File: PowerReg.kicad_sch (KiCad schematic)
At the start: 8 parts

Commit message: Assigned almost all footprints
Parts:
- C44, C46: footprint (none) -> Capacitor_SMD:C_0603_1608Metric; Part # (none) -> Generic 0603 1uF 6.3V X7R MLCC
- C45, C47: footprint (none) -> Capacitor_SMD:C_0603_1608Metric; Part # (none) -> Generic 0603 0.1uF 6.3V X7R MLCC
- U32, U33: footprint (none) -> Converter_DCDC:Converter_DCDC_TRACO_TSR-1_THT
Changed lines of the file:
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@@
 			)
 		)
-		(property "Footprint" ""
+		(property "Footprint" "Capacitor_SMD:C_0603_1608Metric"
 			(at 172.72 97.79 0)
 			(effects
@@
 		)
 		(property "Description" "Unpolarized capacitor, small symbol"
+			(at 172.72 97.79 0)
+			(effects
+				(font
+					(size 1.27 1.27)
+				)
+				(hide yes)
+			)
+		)
+		(property "Part #" "Generic 0603 1uF 6.3V X7R MLCC"
 			(at 172.72 97.79 0)
 			(effects
@@
 			)
 		)
-		(property "Footprint" ""
+		(property "Footprint" "Capacitor_SMD:C_0603_1608Metric"
 			(at 149.86 97.79 0)
 			(effects
@@
 		)
 		(property "Description" "Unpolarized capacitor, small symbol"
+			(at 149.86 97.79 0)
+			(effects
+				(font
+					(size 1.27 1.27)
+				)
+				(hide yes)
+			)
+		)
+		(property "Part #" "Generic 0603 0.1uF 6.3V X7R MLCC"
 			(at 149.86 97.79 0)
 			(effects
@@
 			)
 		)
-		(property "Footprint" ""
+		(property "Footprint" "Capacitor_SMD:C_0603_1608Metric"
 			(at 193.04 97.79 0)
 			(effects
@@
 		)
 		(property "Description" "Unpolarized capacitor, small symbol"
+			(at 193.04 97.79 0)
+			(effects
+				(font
+					(size 1.27 1.27)
+				)
+				(hide yes)
+			)
+		)
+		(property "Part #" "Generic 0603 0.1uF 6.3V X7R MLCC"
 			(at 193.04 97.79 0)
 			(effects
@@
 			)
 		)
-		(property "Footprint" ""
+		(property "Footprint" "Capacitor_SMD:C_0603_1608Metric"
 			(at 129.54 97.79 0)
 			(effects
@@
 		)
 		(property "Description" "Unpolarized capacitor, small symbol"
+			(at 129.54 97.79 0)
+			(effects
+				(font
+					(size 1.27 1.27)
+				)
+				(hide yes)
+			)
+		)
+		(property "Part #" "Generic 0603 1uF 6.3V X7R MLCC"
 			(at 129.54 97.79 0)
 			(effects
@@
 			)
 		)
-		(property "Footprint" ""
+		(property "Footprint" "Converter_DCDC:Converter_DCDC_TRACO_TSR-1_THT"
 			(at 139.7 85.09 0)
 			(effects
@@
 			)
 		)
-		(property "Footprint" ""
+		(property "Footprint" "Converter_DCDC:Converter_DCDC_TRACO_TSR-1_THT"
 			(at 182.88 85.09 0)
 			(effects

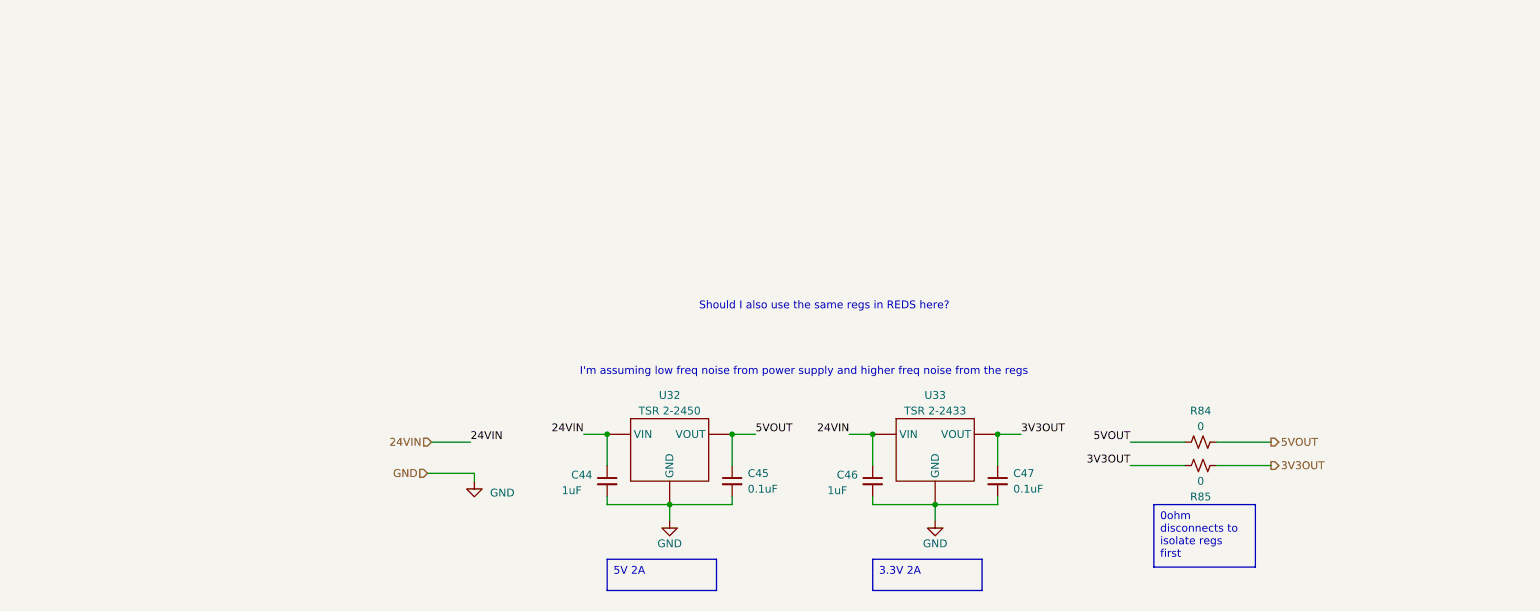
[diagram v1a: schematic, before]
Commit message: Replaced Regs
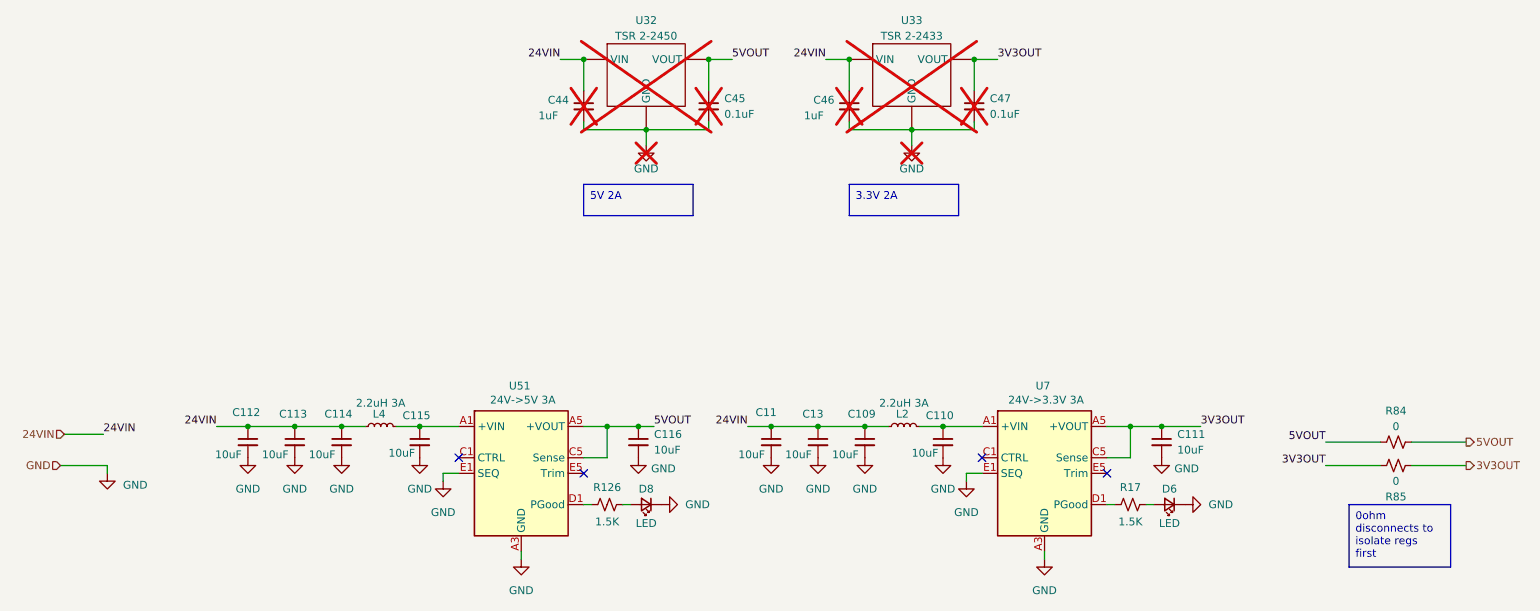
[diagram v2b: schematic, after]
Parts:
- added C109, C11, C110, C112, C113, C114, C115, C13: 10uF, Capacitor_SMD:C_1210_3225Metric, symbol Device:C_Small
- added C111, C116: 10uF, Capacitor_SMD:C_1206_3216Metric, symbol Device:C_Small
- added D6, D8: LED, LED_SMD:LED_0603_1608Metric_Pad1.05x0.95mm_HandSolder, symbol Device:LED_Small
- added L2, L4: 2.2uH 3A, Inductor_SMD:L_Vishay_IHLP-1212, symbol Device:L_Small
- added R126, R17: 1.5K, Resistor_SMD:R_0402_1005Metric, symbol Device:R_Small_US
- added U51: 24V->5V 3A, Converter_DCDC:Converter_DCDC_RECOM_RPMx.x-x.0, symbol Converter_DCDC:RPM3.3-6.0
- added U7: 24V->3.3V 3A, Converter_DCDC:Converter_DCDC_RECOM_RPMx.x-x.0, symbol Converter_DCDC:RPM3.3-6.0
- C44, C45, C46, C47, U32, U33: now not fitted; now left out of the parts list
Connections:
- net 24VIN: now also C109.1, C11.1, C112.1, C113.1, C114.1, C13.1, L2.1, L4.1
- net 3V3OUT: now also C111.1, U7.A5 (+VOUT), U7.B5 (+VOUT), U7.C5 (Sense)
- net 5VOUT: now also C116.1, U51.A5 (+VOUT), U51.B5 (+VOUT), U51.C5 (Sense)
- net GND: now also C109.2, C11.2, C110.2, C111.2, C112.2, C113.2, C114.2, C115.2, C116.2, C13.2, D6.1 (K), D8.1 (K), U51.A3 (GND), U51.A4 (GND), U51.B1 (GND), U51.B2 (GND), U51.B3 (GND), U51.B4 (GND), U51.C2 (GND), U51.C3 (GND), U51.C4 (GND), U51.D2 (GND), U51.D3 (GND), U51.D4 (GND), U51.D5 (GND), U51.E1 (SEQ), U51.E3 (GND), U51.E4 (GND), U7.A3 (GND), U7.A4 (GND), U7.B1 (GND), U7.B2 (GND), U7.B3 (GND), U7.B4 (GND), U7.C2 (GND), U7.C3 (GND), U7.C4 (GND), U7.D2 (GND), U7.D3 (GND), U7.D4 (GND), U7.D5 (GND), U7.E1 (SEQ), U7.E3 (GND), U7.E4 (GND)
- new net: C110.1, L2.2, U7.A1 (+VIN), U7.A2 (+VIN)
- new net: C115.1, L4.2, U51.A1 (+VIN), U51.A2 (+VIN)
- new net: R126.1, U51.D1 (PGood)
- new net: D8.2 (A), R126.2
- new net: D6.2 (A), R17.2
- new net: R17.1, U7.D1 (PGood)
- no-connect marks 0 -> 4
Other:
- note removed: "I'm assuming low freq noise from power supply and higher freq noise from the regs"
- note removed: "Should I also use the same regs in REDS here?"
- moved on the sheet: R84, R85

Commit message: Finished layout
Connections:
- net 3V3OUT: no longer C111.1, R85.1, U7.A5 (+VOUT), U7.B5 (+VOUT), U7.C5 (Sense)
- net 5VOUT: no longer C116.1, R84.1, U51.A5 (+VOUT), U51.B5 (+VOUT), U51.C5 (Sense)
- new net: C111.1, R85.1, U7.A5 (+VOUT), U7.B5 (+VOUT), U7.C5 (Sense)
- new net: C116.1, R84.1, U51.A5 (+VOUT), U51.B5 (+VOUT), U51.C5 (Sense)
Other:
- moved on the sheet: R84, R85
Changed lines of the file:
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@@
 	(wire
 		(pts
-			(xy 134.62 88.9) (xy 137.16 88.9)
+			(xy 134.62 88.9) (xy 135.89 88.9)
 		)
 		(stroke
@@
 	(wire
 		(pts
-			(xy 260.35 91.44) (xy 269.24 91.44)
+			(xy 149.86 81.28) (xy 158.75 81.28)
 		)
 		(stroke
@@
 	(wire
 		(pts
-			(xy 219.71 88.9) (xy 226.06 88.9)
+			(xy 135.89 81.28) (xy 135.89 88.9)
+		)
+		(stroke
+			(width 0)
+			(type default)
+		)
+	)
+	(wire
+		(pts
+			(xy 219.71 88.9) (xy 238.76 88.9)
 		)
 		(stroke
@@
 	(wire
 		(pts
-			(xy 246.38 91.44) (xy 255.27 91.44)
+			(xy 135.89 81.28) (xy 144.78 81.28)
 		)
 		(stroke
@@
 	(wire
 		(pts
-			(xy 246.38 95.25) (xy 255.27 95.25)
-		)
-		(stroke
-			(width 0)
-			(type default)
-		)
-	)
-	(wire
-		(pts
-			(xy 260.35 95.25) (xy 269.24 95.25)
+			(xy 243.84 88.9) (xy 252.73 88.9)
 		)
 		(stroke
@@
 	(text_box "0ohm disconnects to isolate regs first"
 		(exclude_from_sim no)
-		(at 250.19 101.6 0)
+		(at 233.68 95.25 0)
 		(size 16.51 10.16)
 		(stroke
@@
 	)
 	(label "3V3OUT"
-		(at 246.38 95.25 180)
+		(at 193.04 29.21 0)
 		(fields_autoplaced yes)
 		(effects
@@
 				(size 1.27 1.27)
 			)
-			(justify right bottom)
-		)
-	)
-	(label "5VOUT"
-		(at 246.38 91.44 180)
+			(justify left bottom)
+		)
+	)
+	(label "24VIN"
+		(at 121.92 29.21 180)
 		(fields_autoplaced yes)
 		(effects
@@
 		)
 	)
-	(label "3V3OUT"
-		(at 193.04 29.21 0)
+	(label "24VIN"
+		(at 47.625 90.17 0)
 		(fields_autoplaced yes)
 		(effects
@@
 		)
 	)
-	(label "5VOUT"
-		(at 137.16 88.9 0)
+	(label "24VIN"
+		(at 165.1 29.21 180)
 		(fields_autoplaced yes)
 		(effects
@@
 				(size 1.27 1.27)
 			)
-			(justify left bottom)
+			(justify right bottom)
 		)
 	)
 	(label "24VIN"
-		(at 121.92 29.21 180)
+		(at 66.04 88.9 180)
 		(fields_autoplaced yes)
 		(effects
@@
 		)
 	)
-	(label "24VIN"
-		(at 47.625 90.17 0)
+	(label "5VOUT"
+		(at 149.86 29.21 0)
 		(fields_autoplaced yes)
 		(effects
@@
 		)
 	)
-	(label "3V3OUT"
-		(at 226.06 88.9 0)
+	(hierarchical_label "5VOUT"
+		(shape output)
+		(at 158.75 81.28 0)
 		(fields_autoplaced yes)
 		(effects
@@
 				(size 1.27 1.27)
 			)
-			(justify left bottom)
-		)
-	)
-	(label "24VIN"
-		(at 165.1 29.21 180)
+			(justify left)
+		)
+	)
+	(hierarchical_label "24VIN"
+		(shape input)
+		(at 41.275 90.17 180)
 		(fields_autoplaced yes)
 		(effects
@@
 				(size 1.27 1.27)
 			)
-			(justify right bottom)
-		)
-	)
-	(label "24VIN"
-		(at 66.04 88.9 180)
-		(fields_autoplaced yes)
-		(effects
-			(font
-				(size 1.27 1.27)
-			)
-			(justify right bottom)
-		)
-	)
-	(label "5VOUT"
-		(at 149.86 29.21 0)
-		(fields_autoplaced yes)
-		(effects
-			(font
-				(size 1.27 1.27)
-			)
-			(justify left bottom)
-		)
-	)
-	(hierarchical_label "5VOUT"
-		(shape output)
-		(at 269.24 91.44 0)
-		(fields_autoplaced yes)
-		(effects
-			(font
-				(size 1.27 1.27)
-			)
-			(justify left)
-		)
-	)
-	(hierarchical_label "24VIN"
-		(shape input)
-		(at 41.275 90.17 180)
-		(fields_autoplaced yes)
-		(effects
-			(font
-				(size 1.27 1.27)
-			)
 			(justify right)
 		)
@@
 	(hierarchical_label "3V3OUT"
 		(shape output)
-		(at 269.24 95.25 0)
+		(at 252.73 88.9 0)
 		(fields_autoplaced yes)
 		(effects
@@
 	(symbol
 		(lib_id "Device:R_Small_US")
-		(at 257.81 95.25 90)
+		(at 241.3 88.9 90)
 		(unit 1)
 		(exclude_from_sim no)
@@
 		(dnp no)
 		(property "Reference" "R85"
-			(at 257.81 100.33 90)
+			(at 241.3 93.98 90)
 			(effects
 				(font
@@
 		)
 		(property "Value" "0"
-			(at 257.81 97.79 90)
+			(at 241.3 91.44 90)
 			(effects
 				(font
@@
 		)
 		(property "Footprint" "Resistor_SMD:R_1206_3216Metric_Pad1.30x1.75mm_HandSolder"
-			(at 257.81 95.25 0)
+			(at 241.3 88.9 0)
 			(effects
 				(font
@@
 		)
 		(property "Datasheet" "~"
-			(at 257.81 95.25 0)
+			(at 241.3 88.9 0)
 			(effects
 				(font
@@
 		)
 		(property "Description" ""
-			(at 257.81 95.25 0)
+			(at 241.3 88.9 0)
 			(effects
 				(font
@@
 	(symbol
 		(lib_id "Device:R_Small_US")
-		(at 257.81 91.44 90)
+		(at 147.32 81.28 90)
 		(unit 1)
 		(exclude_from_sim no)
@@
 		(on_board yes)
 		(dnp no)
-		(fields_autoplaced yes)
 		(property "Reference" "R84"
-			(at 257.81 86.36 90)
+			(at 147.32 76.2 90)
 			(effects
 				(font
@@
 		)
 		(property "Value" "0"
-			(at 257.81 88.9 90)
+			(at 147.32 78.74 90)
 			(effects
 				(font
@@
 		)
 		(property "Footprint" "Resistor_SMD:R_1206_3216Metric_Pad1.30x1.75mm_HandSolder"
-			(at 257.81 91.44 0)
+			(at 147.32 81.28 0)
 			(effects
 				(font
@@
 		)
 		(property "Datasheet" "~"
-			(at 257.81 91.44 0)
+			(at 147.32 81.28 0)
 			(effects
 				(font
@@
 		)
 		(property "Description" ""
-			(at 257.81 91.44 0)
-			(effects
-				(font
+			(at 147.32 81.28 0)
+			(effects
+				(font

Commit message: new BOM
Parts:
- C109, C11, C110, C112, C113, C114, C115, C13: Manufacturer (none) -> Generic; Part # (none) -> Generic CAP CER 10UF 50V X7R 1210
- C111, C116: Manufacturer (none) -> Generic; Part # (none) -> Generic CAP CER 10UF 25V X7R 1206
- C44, C46: Manufacturer (none) -> Generic; Part # Generic 0603 1uF 6.3V X7R MLCC -> Generic CAP CER 1UF 50V X7R 0603
- C45, C47: Manufacturer (none) -> Generic; Part # Generic 0603 0.1uF 6.3V X7R MLCC -> Generic CAP CER 0.1UF 6.3V X7R 0603
- R126, R17: Part # Generic 0402 1.5K 0.1% Resistor -> Generic RES SMD 1.5K OHM 0.1% 1/16W 0402
- R84, R85: Manufacturer (none) -> Generic; Part # (none) -> Generic RES SMD 0 OHM 1206
- U51, U7: Manufacturer RECOM -> Recom Power

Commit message: REDS updated with diodes and hierarchy to main micro
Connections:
- net 3V3OUT renamed 3V3_REDSOUT

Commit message: Component placement halfway done
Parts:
- added TP25: 5V, TestPoint:TestPoint_Plated_Hole_D2.0mm, symbol Connector:TestPoint
- added TP26: 3.3V, TestPoint:TestPoint_Plated_Hole_D2.0mm, symbol Connector:TestPoint
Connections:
- net at C111.1, R85.1, U7.A5 (+VOUT)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: now also TP26.1
- net at C116.1, R84.1, U51.A5 (+VOUT)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: now also TP25.1
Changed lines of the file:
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@@
 		(color 0 0 0 0)
 	)
+	(junction
+		(at 135.89 81.28)
+		(diameter 0)
+		(color 0 0 0 0)
+	)
 	(no_connect
 		(at 190.5 93.98)
@@
 	)
 	(symbol
+		(lib_id "Connector:TestPoint")
+		(at 135.89 81.28 0)
+		(unit 1)
+		(exclude_from_sim no)
+		(in_bom yes)
+		(on_board yes)
+		(dnp no)
+		(fields_autoplaced yes)
+		(property "Reference" "TP25"
+			(at 138.43 76.7079 0)
+			(effects
+				(font
+					(size 1.27 1.27)
+				)
+				(justify left)
+			)
+		)
+		(property "Value" "5V"
+			(at 138.43 79.2479 0)
+			(effects
+				(font
+					(size 1.27 1.27)
+				)
+				(justify left)
+			)
+		)
+		(property "Footprint" "TestPoint:TestPoint_Plated_Hole_D2.0mm"
+			(at 140.97 81.28 0)
+			(effects
+				(font
+					(size 1.27 1.27)
+				)
+				(hide yes)
+			)
+		)
+		(property "Datasheet" "~"
+			(at 140.97 81.28 0)
+			(effects
+				(font
+					(size 1.27 1.27)
+				)
+				(hide yes)
+			)
+		)
+		(property "Description" "test point"
+			(at 135.89 81.28 0)
+			(effects
+				(font
+					(size 1.27 1.27)
+				)
+				(hide yes)
+			)
+		)
+		(pin "1"
+		)
+		(instances
+			(project "rocket2-ecu"
+				(path "/02606b2c-b376-4ffb-9781-f9cea3f70994/944e98dc-4249-4ad7-a352-e05a5cc42499"
+					(reference "TP25")
+					(unit 1)
+				)
+			)
+		)
+	)
+	(symbol
 		(lib_id "Device:R_Small_US")
 		(at 241.3 88.9 90)
@@
 					(unit 1)
 				)
+			)
+		)
+	)
+	(symbol
+		(lib_id "Connector:TestPoint")
+		(at 219.71 88.9 0)
+		(unit 1)
+		(exclude_from_sim no)
+		(in_bom yes)
+		(on_board yes)
+		(dnp no)
+		(fields_autoplaced yes)
+		(property "Reference" "TP26"
+			(at 222.25 84.3279 0)
+			(effects
+				(font
+					(size 1.27 1.27)
+				)
+				(justify left)
+			)
+		)
+		(property "Value" "3.3V"
+			(at 222.25 86.8679 0)
+			(effects
+				(font
+					(size 1.27 1.27)
+				)
+				(justify left)
+			)
+		)
+		(property "Footprint" "TestPoint:TestPoint_Plated_Hole_D2.0mm"
+			(at 224.79 88.9 0)
+			(effects
+				(font
+					(size 1.27 1.27)
+				)
+				(hide yes)
+			)
+		)
+		(property "Datasheet" "~"
+			(at 224.79 88.9 0)
+			(effects
+				(font
+					(size 1.27 1.27)
+				)
+				(hide yes)
+			)
+		)
+		(property "Description" "test point"
+			(at 219.71 88.9 0)
+			(effects
+				(font
+					(size 1.27 1.27)
+				)
+				(hide yes)
+			)
+		)
+		(pin "1"
+		)
+		(instances
+			(project "rocket2-ecu"
+				(path "/02606b2c-b376-4ffb-9781-f9cea3f70994/944e98dc-4249-4ad7-a352-e05a5cc42499"
+					(reference "TP26")
+					(unit 1)
+				)

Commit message: ALMOST
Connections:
- net 3.3V_out: now reaches C111.1, R85.1, TP26.1, U7.A5 (+VOUT), U7.B5 (+VOUT), U7.C5 (Sense)
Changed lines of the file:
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@@
+		(color 0 0 0 0)
+	)
+	(junction
+		(at 231.14 88.9)
+		(diameter 0)
 		(color 0 0 0 0)
 	)
@@
 	(wire
 		(pts
+			(xy 231.14 88.9) (xy 238.76 88.9)
+		)
+		(stroke
+			(width 0)
+			(type default)
+		)
+	)
+	(wire
+		(pts
 			(xy 165.1 29.21) (xy 168.91 29.21)
 		)
@@
 	(wire
 		(pts
-			(xy 219.71 88.9) (xy 238.76 88.9)
+			(xy 219.71 88.9) (xy 231.14 88.9)
 		)
 		(stroke
@@
 					(unit 1)
 				)
+			)
+		)
+	)
+	(symbol
+		(lib_id "power:+1V5")
+		(at 231.14 88.9 0)
+		(unit 1)
+		(exclude_from_sim no)
+		(in_bom yes)
+		(on_board yes)
+		(dnp no)
+		(fields_autoplaced yes)
+		(property "Reference" "#PWR0296"
+			(at 231.14 92.71 0)
+			(effects
+				(font
+					(size 1.27 1.27)
+				)
+				(hide yes)
+			)
+		)
+		(property "Value" "3.3V_out"
+			(at 231.14 83.82 0)
+			(effects
+				(font
+					(size 1.27 1.27)
+				)
+			)
+		)
+		(property "Footprint" ""
+			(at 231.14 88.9 0)
+			(effects
+				(font
+					(size 1.27 1.27)
+				)
+				(hide yes)
+			)
+		)
+		(property "Datasheet" ""
+			(at 231.14 88.9 0)
+			(effects
+				(font
+					(size 1.27 1.27)
+				)
+				(hide yes)
+			)
+		)
+		(property "Description" "Power symbol creates a global label with name \"+1V5\""
+			(at 231.14 88.9 0)
+			(effects
+				(font
+					(size 1.27 1.27)
+				)
+				(hide yes)
+			)
+		)
+		(pin "1"
+		)
+		(instances
+			(project ""
+				(path "/02606b2c-b376-4ffb-9781-f9cea3f70994/944e98dc-4249-4ad7-a352-e05a5cc42499"
+					(reference "#PWR0296")
+					(unit 1)
+				)

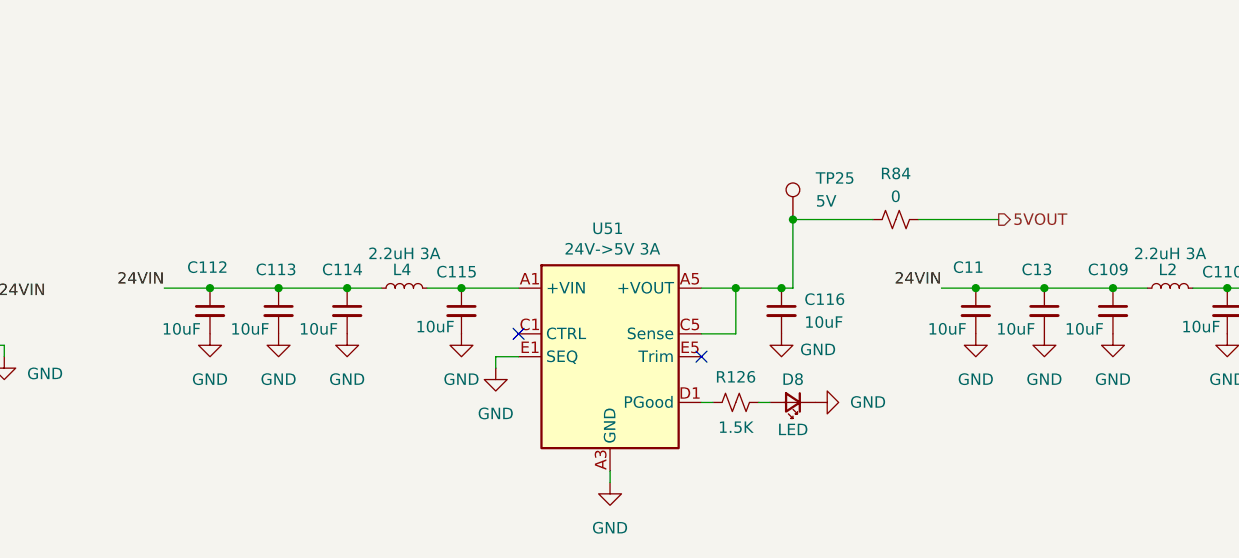
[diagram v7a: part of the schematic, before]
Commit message: Deleted 5V, edited LPFs on TCs and PTs
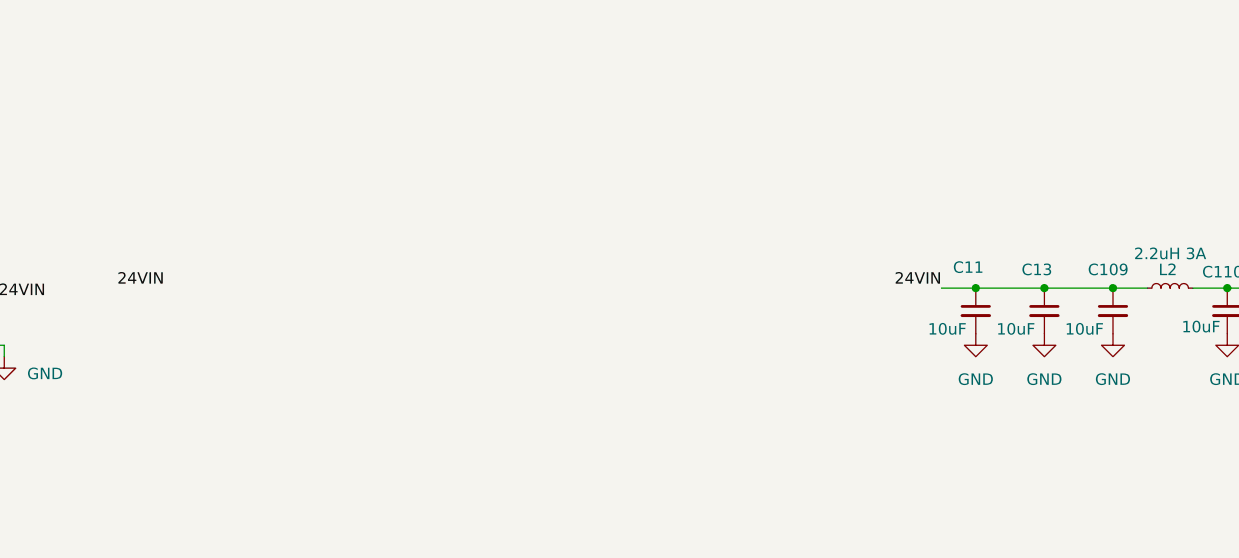
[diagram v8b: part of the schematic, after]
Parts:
- removed C112, C113, C114, C115: 10uF, Capacitor_SMD:C_1210_3225Metric, symbol Device:C_Small
- removed C116: 10uF, Capacitor_SMD:C_1206_3216Metric, symbol Device:C_Small
- removed D8: LED, LED_SMD:LED_0603_1608Metric_Pad1.05x0.95mm_HandSolder, symbol Device:LED_Small
- removed L4: 2.2uH 3A, Inductor_SMD:L_Vishay_IHLP-1212, symbol Device:L_Small
- removed R126: 1.5K, Resistor_SMD:R_0402_1005Metric, symbol Device:R_Small_US
- removed R84: 0, Resistor_SMD:R_1206_3216Metric_Pad1.30x1.75mm_HandSolder, symbol Device:R_Small_US
- removed TP25: 5V, TestPoint:TestPoint_Plated_Hole_D2.0mm, symbol Connector:TestPoint
- removed U51: 24V->5V 3A, Converter_DCDC:Converter_DCDC_RECOM_RPMx.x-x.0, symbol Converter_DCDC:RPM3.3-6.0
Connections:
- no-connect marks 4 -> 2
